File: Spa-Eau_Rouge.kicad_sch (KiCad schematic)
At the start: 3 parts, among them J1 XT30PW-M, J2 SM02B-GHS-TB, J3 PH1RA-03-UA

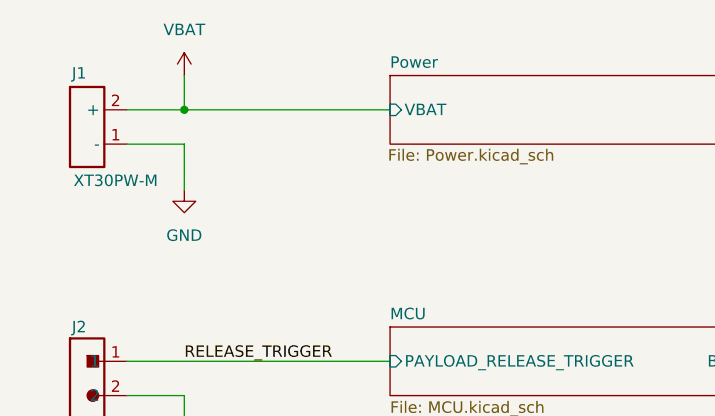
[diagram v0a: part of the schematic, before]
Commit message: added CMC, TVS diode, electrolytic cap at buck input to improve inrush current effects
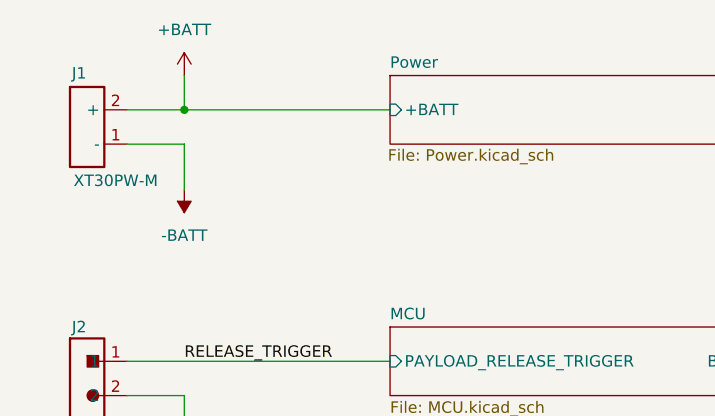
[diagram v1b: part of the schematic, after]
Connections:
- net GND: no longer J1.1 (-)
- net VBAT renamed +BATT
- new net -BATT: J1.1 (-)
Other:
- sheet Power ports: added +BATT; removed VBAT
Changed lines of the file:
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@@
+	)
+	(symbol
+		(lib_id "power:+BATT")
+		(at 88.9 101.6 0)
+		(unit 1)
+		(exclude_from_sim no)
+		(in_bom yes)
+		(on_board yes)
+		(dnp no)
+		(fields_autoplaced yes)
+		(property "Reference" "#PWR020"
+			(at 88.9 105.41 0)
+			(effects
+				(font
+					(size 1.27 1.27)
+				)
+				(hide yes)
+			)
+		)
+		(property "Value" "+BATT"
+			(at 88.9 96.52 0)
+			(effects
+				(font
+					(size 1.27 1.27)
+				)
+			)
+		)
+		(property "Footprint" ""
+			(at 88.9 101.6 0)
+			(effects
+				(font
+					(size 1.27 1.27)
+				)
+				(hide yes)
+			)
+		)
+		(property "Datasheet" ""
+			(at 88.9 101.6 0)
+			(effects
+				(font
+					(size 1.27 1.27)
+				)
+				(hide yes)
+			)
+		)
+		(property "Description" "Power symbol creates a global label with name \"+BATT\""
+			(at 88.9 101.6 0)
+			(effects
+				(font
+					(size 1.27 1.27)
+				)
+				(hide yes)
+			)
+		)
+		(pin "1"
+		)
+		(instances
+			(project ""
+				(path "/c4971751-18ba-42c0-933f-7e935423e3d9"
+					(reference "#PWR020")
+					(unit 1)
+				)
+			)
+		)
 	)
 	(symbol
@@
 	)
 	(symbol
-		(lib_id "power:VBAT")
-		(at 88.9 101.6 0)
-		(unit 1)
-		(exclude_from_sim no)
-		(in_bom yes)
-		(on_board yes)
-		(dnp no)
-		(property "Reference" "#PWR020"
-			(at 88.9 105.41 0)
-			(effects
-				(font
-					(size 1.27 1.27)
-				)
-				(hide yes)
-			)
-		)
-		(property "Value" "VBAT"
-			(at 88.9 96.52 0)
+		(lib_id "power:-BATT")
+		(at 88.9 114.3 180)
+		(unit 1)
+		(exclude_from_sim no)
+		(in_bom yes)
+		(on_board yes)
+		(dnp no)
+		(fields_autoplaced yes)
+		(property "Reference" "#PWR018"
+			(at 88.9 110.49 0)
+			(effects
+				(font
+					(size 1.27 1.27)
+				)
+				(hide yes)
+			)
+		)
+		(property "Value" "-BATT"
+			(at 88.9 119.38 0)
 			(effects
 				(font
@@
 		)
 		(property "Footprint" ""
-			(at 88.9 101.6 0)
-			(effects
-				(font
-					(size 1.27 1.27)
-				)
-				(hide yes)
-			)
-		)
-		(property "Datasheet" ""
-			(at 88.9 101.6 0)
-			(effects
-				(font
-					(size 1.27 1.27)
-				)
-				(hide yes)
-			)
-		)
-		(property "Description" "Power symbol creates a global label with name \"VBAT\""
-			(at 88.9 101.6 0)
+			(at 88.9 114.3 0)
+			(effects
+				(font
+					(size 1.27 1.27)
+				)
+				(hide yes)
+			)
+		)
+		(property "Datasheet" ""
+			(at 88.9 114.3 0)
+			(effects
+				(font
+					(size 1.27 1.27)
+				)
+				(hide yes)
+			)
+		)
+		(property "Description" "Power symbol creates a global label with name \"-BATT\""
+			(at 88.9 114.3 0)
 			(effects
 				(font
@@
 			(project ""
 				(path "/c4971751-18ba-42c0-933f-7e935423e3d9"
-					(reference "#PWR020")
+					(reference "#PWR018")
 					(unit 1)
 				)
@@
 				(path "/c4971751-18ba-42c0-933f-7e935423e3d9"
 					(reference "#PWR023")
-					(unit 1)
-				)
-			)
-		)
-	)
-	(symbol
-		(lib_id "power:GND")
-		(at 88.9 114.3 0)
-		(unit 1)
-		(exclude_from_sim no)
-		(in_bom yes)
-		(on_board yes)
-		(dnp no)
-		(fields_autoplaced yes)
-		(property "Reference" "#PWR021"
-			(at 88.9 120.65 0)
-			(effects
-				(font
-					(size 1.27 1.27)
-				)
-				(hide yes)
-			)
-		)
-		(property "Value" "GND"
-			(at 88.9 119.38 0)
-			(effects
-				(font
-					(size 1.27 1.27)
-				)
-			)
-		)
-		(property "Footprint" ""
-			(at 88.9 114.3 0)
-			(effects
-				(font
-					(size 1.27 1.27)
-				)
-				(hide yes)
-			)
-		)
-		(property "Datasheet" ""
-			(at 88.9 114.3 0)
-			(effects
-				(font
-					(size 1.27 1.27)
-				)
-				(hide yes)
-			)
-		)
-		(property "Description" "Power symbol creates a global label with name \"GND\" , ground"
-			(at 88.9 114.3 0)
-			(effects
-				(font
-					(size 1.27 1.27)
-				)
-				(hide yes)
-			)
-		)
-		(pin "1"
-		)
-		(instances
-			(project ""
-				(path "/c4971751-18ba-42c0-933f-7e935423e3d9"
-					(reference "#PWR021")
 					(unit 1)
 				)
@@
 			)
 		)
-		(pin "VBAT" input
+		(pin "+BATT" input
 			(at 111.76 105.41 180)
 			(effects

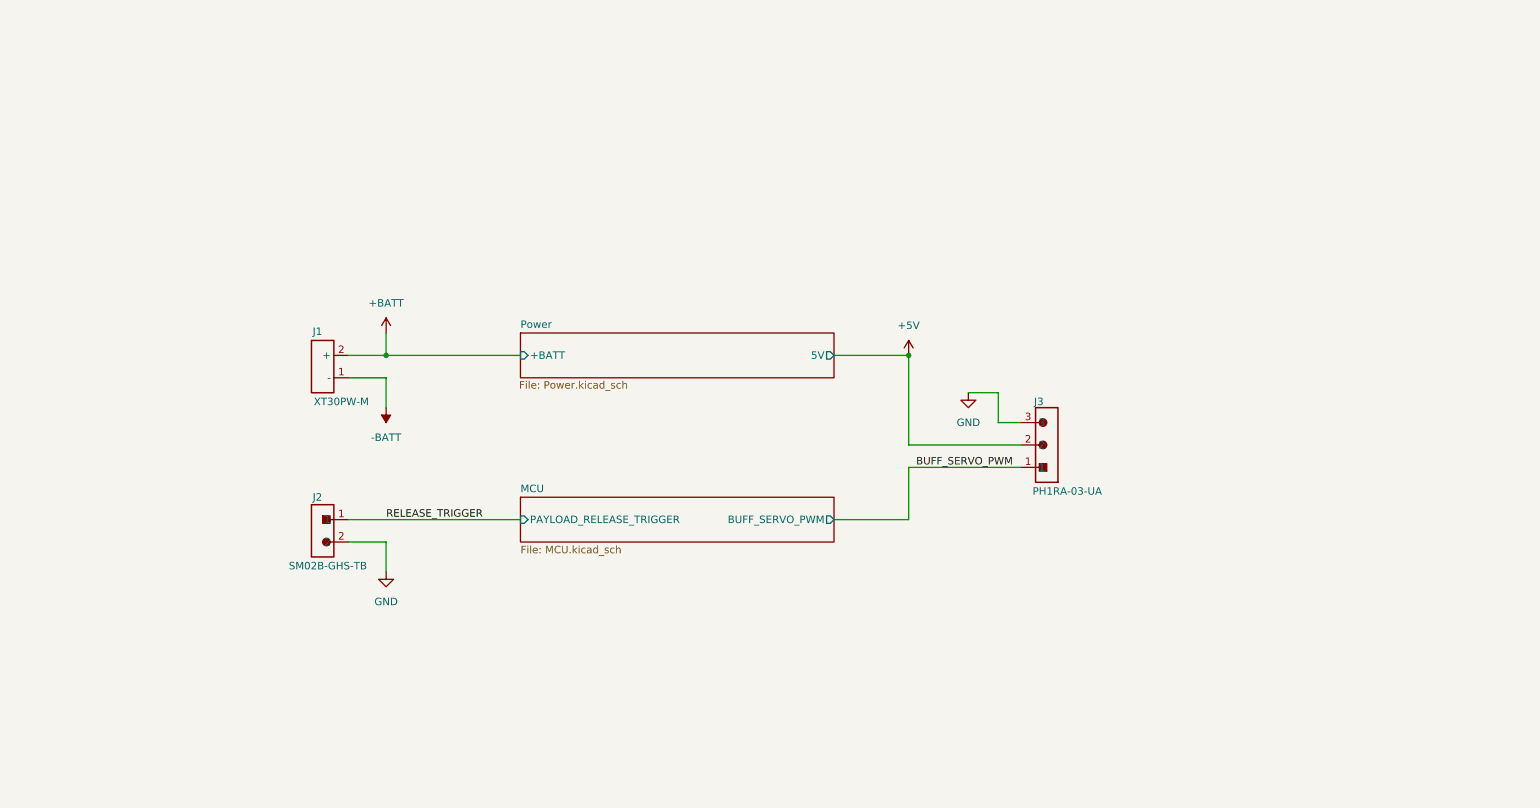
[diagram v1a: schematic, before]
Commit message: Added solenoid driver circuit
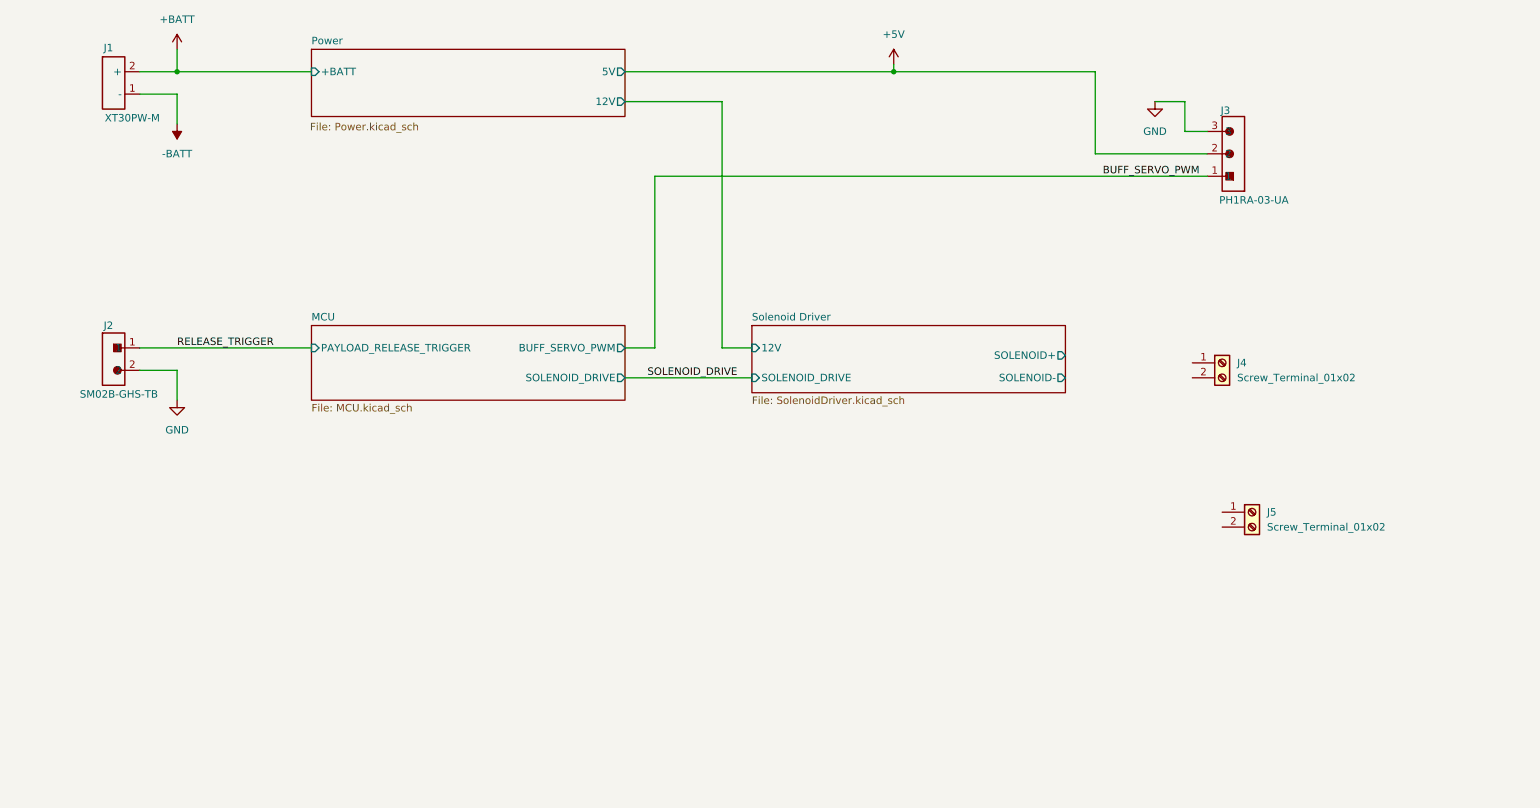
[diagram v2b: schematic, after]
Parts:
- added J4: Screw_Terminal_01x02, symbol Connector:Screw_Terminal_01x02
- added J5: Screw_Terminal_01x02, TerminalBlock_Phoenix:TerminalBlock_Phoenix_PT-1,5-2-3.5-H_1x02_P3.50mm_Horizontal, symbol Connector:Screw_Terminal_01x02
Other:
- added sheet Solenoid Driver (SolenoidDriver.kicad_sch)
- sheet MCU ports: added SOLENOID_DRIVE; removed none
- sheet Power ports: added 12V; removed none
- moved on the sheet: J1, J2, J3

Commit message: 1st round of rough component placement
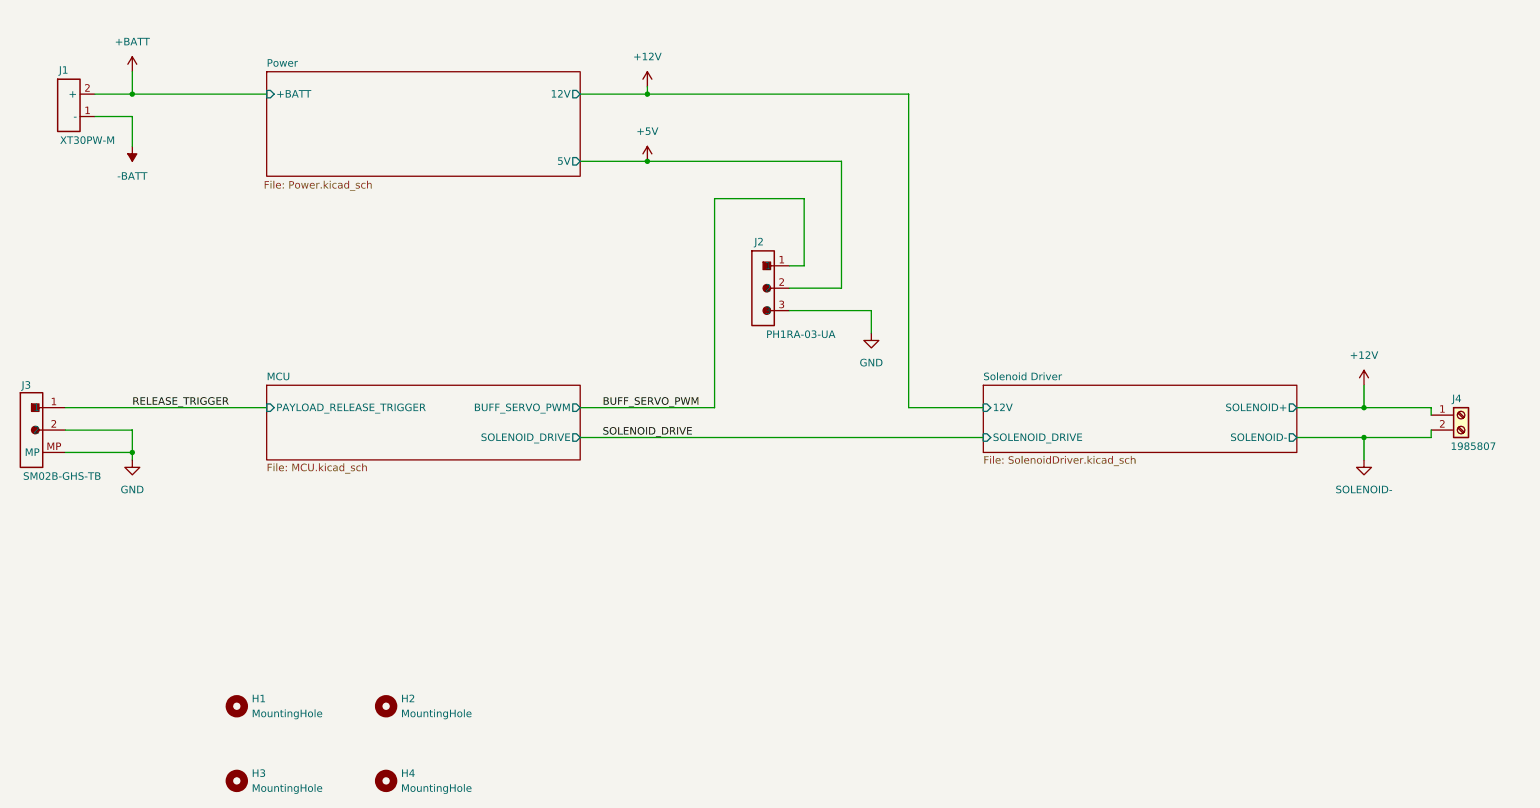
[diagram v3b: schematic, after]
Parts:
- removed J3: PH1RA-03-UA, Connector_PinHeader_2.54mm:PinHeader_1x03_P2.54mm_Horizontal, symbol Connector:Conn-1x03-2.54mm-RA_PH1RA-03-UA
- removed J4: Screw_Terminal_01x02, symbol Connector:Screw_Terminal_01x02
- removed J5: Screw_Terminal_01x02, TerminalBlock_Phoenix:TerminalBlock_Phoenix_PT-1,5-2-3.5-H_1x02_P3.50mm_Horizontal, symbol Connector:Screw_Terminal_01x02
- added H1, H2, H3, H4: MountingHole, MountingHole:MountingHole_3.2mm_M3, symbol Mechanical:MountingHole
- added J2: PH1RA-03-UA, Connector_PinHeader_2.54mm:PinHeader_1x03_P2.54mm_Horizontal, symbol Connector:Conn-1x03-2.54mm-RA_PH1RA-03-UA
- added J4: 1985807, TerminalBlock_Phoenix:TerminalBlock_Phoenix_MKDS-1,5-2_1x02_P3.50mm_Horizontal_1985807, symbol Connector:Screw_Terminal_01x02_1985807
- renumbered J2 to J3
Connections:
- net +5V: now also J2.2
- net BUFF_SERVO_PWM: now also J2.1
- net GND: now also J3.MP, J2.3
- new net +12V: J4.1 (Pin_1)
- new net SOLENOID-: J4.2 (Pin_2)
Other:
- moved on the sheet: J1

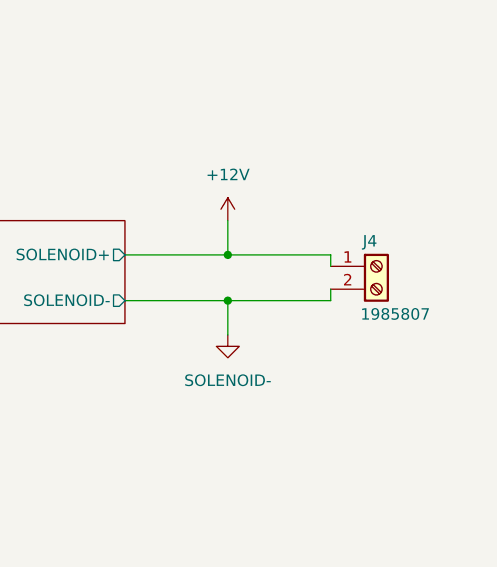
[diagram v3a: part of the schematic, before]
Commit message: pcb routing completed
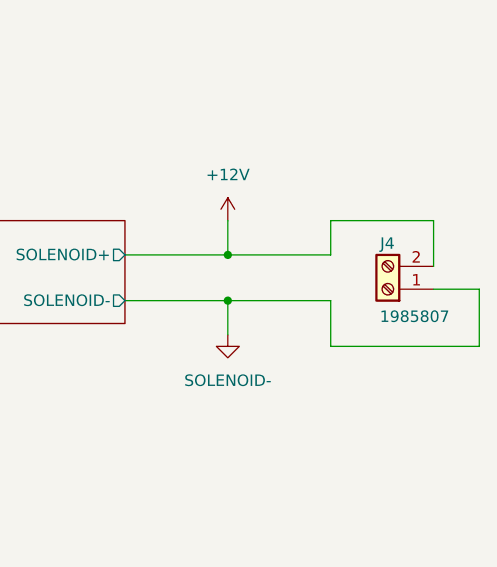
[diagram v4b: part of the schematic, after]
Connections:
- net +12V: now also J4.2 (Pin_2); no longer J4.1 (Pin_1)
- net SOLENOID-: now also J4.1 (Pin_1); no longer J4.2 (Pin_2)
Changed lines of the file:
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@@
-	(wire
-		(pts
-			(xy 266.7 118.11) (xy 266.7 119.38)
-		)
-		(stroke
-			(width 0)
-			(type default)
-		)
-	)
 	(wire
 		(pts
@@
 	(wire
 		(pts
+			(xy 266.7 110.49) (xy 278.13 110.49)
+		)
+		(stroke
+			(width 0)
+			(type default)
+		)
+	)
+	(wire
+		(pts
 			(xy 255.27 114.3) (xy 266.7 114.3)
 		)
@@
 	(wire
 		(pts
+			(xy 283.21 118.11) (xy 278.13 118.11)
+		)
+		(stroke
+			(width 0)
+			(type default)
+		)
+	)
+	(wire
+		(pts
 			(xy 190.5 114.3) (xy 177.8 114.3)
 		)
@@
 	(wire
 		(pts
+			(xy 283.21 118.11) (xy 283.21 124.46)
+		)
+		(stroke
+			(width 0)
+			(type default)
+		)
+	)
+	(wire
+		(pts
+			(xy 266.7 124.46) (xy 266.7 119.38)
+		)
+		(stroke
+			(width 0)
+			(type default)
+		)
+	)
+	(wire
+		(pts
 			(xy 68.58 60.96) (xy 45.72 60.96)
 		)
@@
 	(wire
 		(pts
+			(xy 278.13 110.49) (xy 278.13 115.57)
+		)
+		(stroke
+			(width 0)
+			(type default)
+		)
+	)
+	(wire
+		(pts
 			(xy 160.02 78.74) (xy 160.02 90.17)
 		)
@@
 	(wire
 		(pts
-			(xy 266.7 114.3) (xy 266.7 115.57)
-		)
-		(stroke
-			(width 0)
-			(type default)
-		)
-	)
-	(wire
-		(pts
 			(xy 177.8 114.3) (xy 177.8 60.96)
 		)
@@
 	(wire
 		(pts
+			(xy 283.21 124.46) (xy 266.7 124.46)
+		)
+		(stroke
+			(width 0)
+			(type default)
+		)
+	)
+	(wire
+		(pts
 			(xy 255.27 119.38) (xy 266.7 119.38)
 		)
@@
 		(pts
 			(xy 45.72 121.92) (xy 45.72 123.19)
+		)
+		(stroke
+			(width 0)
+			(type default)
+		)
+	)
+	(wire
+		(pts
+			(xy 266.7 114.3) (xy 266.7 110.49)
 		)
 		(stroke
@@
 	)
 	(symbol
-		(lib_id "Connector:Screw_Terminal_01x02_1985807")
-		(at 271.78 115.57 0)
-		(unit 1)
-		(exclude_from_sim no)
-		(in_bom yes)
-		(on_board yes)
-		(dnp no)
-		(property "Reference" "J4"
-			(at 270.256 112.776 0)
-			(effects
-				(font
-					(size 1.27 1.27)
-				)
-				(justify left)
-			)
-		)
-		(property "Value" "1985807"
-			(at 270.002 120.904 0)
-			(effects
-				(font
-					(size 1.27 1.27)
-				)
-				(justify left)
-			)
-		)
-		(property "Footprint" "TerminalBlock_Phoenix:TerminalBlock_Phoenix_MKDS-1,5-2_1x02_P3.50mm_Horizontal_1985807"
-			(at 273.05 129.54 0)
-			(effects
-				(font
-					(size 1.27 1.27)
-				)
-				(hide yes)
-			)
-		)
-		(property "Datasheet" ""
-			(at 271.78 115.57 0)
-			(effects
-				(font
-					(size 1.27 1.27)
-				)
-				(hide yes)
-			)
-		)
-		(property "Description" "TERM BLK 2POS SIDE ENT 3.5MM PCB"
-			(at 272.542 126.238 0)
-			(effects
-				(font
-					(size 1.27 1.27)
-				)
-				(hide yes)
-			)
-		)
-		(pin "1"
-		)
-		(pin "2"
-		)
-		(instances
-			(project ""
-				(path "/c4971751-18ba-42c0-933f-7e935423e3d9"
-					(reference "J4")
-					(unit 1)
-				)
-			)
-		)
-	)
-	(symbol
 		(lib_id "Mechanical:MountingHole")
 		(at 88.9 165.1 0)
@@
 					(unit 1)
 				)
+			)
+		)
+	)
+	(symbol
+		(lib_id "Connector:Screw_Terminal_01x02_1985807")
+		(at 273.05 118.11 180)
+		(unit 1)
+		(exclude_from_sim no)
+		(in_bom yes)
+		(on_board yes)
+		(dnp no)
+		(property "Reference" "J4"
+			(at 273.812 113.03 0)
+			(effects
+				(font
+					(size 1.27 1.27)
+				)
+				(justify left)
+			)
+		)
+		(property "Value" "1985807"
+			(at 279.908 121.158 0)
+			(effects
+				(font
+					(size 1.27 1.27)
+				)
+				(justify left)
+			)
+		)
+		(property "Footprint" "TerminalBlock_Phoenix:TerminalBlock_Phoenix_MKDS-1,5-2_1x02_P3.50mm_Horizontal_1985807"
+			(at 271.78 104.14 0)
+			(effects
+				(font
+					(size 1.27 1.27)
+				)
+				(hide yes)
+			)
+		)
+		(property "Datasheet" ""
+			(at 273.05 118.11 0)
+			(effects
+				(font
+					(size 1.27 1.27)
+				)
+				(hide yes)
+			)
+		)
+		(property "Description" "TERM BLK 2POS SIDE ENT 3.5MM PCB"
+			(at 272.288 107.442 0)
+			(effects
+				(font
+					(size 1.27 1.27)
+				)
+				(hide yes)
+			)
+		)
+		(pin "1"
+		)
+		(pin "2"
+		)
+		(instances
+			(project "Spa-Eau_Rouge"
+				(path "/c4971751-18ba-42c0-933f-7e935423e3d9"
+					(reference "J4")
+					(unit 1)
+				)
